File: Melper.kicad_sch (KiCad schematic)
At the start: 41 parts, among them J1 Conn_01x02, J2 Conn_02x08_Odd_Even, J3 Conn_02x08_Odd_Even, J4 Conn_02x08_Odd_Even, J5 Conn_02x08_Odd_Even, J6 Conn_02x08_Odd_Even, U1 LM7805_TO220, U2 cui

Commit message: Update Melper.kicad_sch
Changes LED resistors.
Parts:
- J1: Digi-Key Part 2987-CI3102P1V00-NH-ND -> 900-0022232021-ND
- R1, R3: value 1K -> 10K; Digi-Key Part CF14JT1K00CT-ND -> S10KQCT-ND
- R2: value 1K -> 4.7K; Digi-Key Part CF14JT1K00CT-ND -> S4.7KQCT-ND
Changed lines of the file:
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@@
       (effects (font (size 1.27 1.27)) hide)
     )
-    (property "Digi-Key Part" "2987-CI3102P1V00-NH-ND" (id 4) (at 37.465 47.625 0)
+    (property "Digi-Key Part" "900-0022232021-ND" (id 4) (at 37.465 47.625 0)
+      (effects (font (size 1.27 1.27)) hide)
+    )
+    (property "LCSC Part #" "" (id 5) (at 37.465 47.625 0)
       (effects (font (size 1.27 1.27)) hide)
     )
@@
       (effects (font (size 1.27 1.27)) (justify left))
     )
-    (property "Value" "1K" (id 1) (at 138.811 113.6266 0)
+    (property "Value" "4.7K" (id 1) (at 138.811 113.6266 0)
       (effects (font (size 1.27 1.27)) (justify left))
     )
@@
       (effects (font (size 1.27 1.27)) hide)
     )
-    (property "Digi-Key Part" "CF14JT1K00CT-ND" (id 4) (at 137.16 111.76 0)
+    (property "Digi-Key Part" "S4.7KQCT-ND" (id 4) (at 137.16 111.76 0)
       (effects (font (size 1.27 1.27)) hide)
     )
@@
       (effects (font (size 1.27 1.27)) (justify left))
     )
-    (property "Value" "1K" (id 1) (at 122.936 113.6266 0)
+    (property "Value" "10K" (id 1) (at 122.936 113.6266 0)
       (effects (font (size 1.27 1.27)) (justify left))
     )
@@
       (effects (font (size 1.27 1.27)) hide)
     )
-    (property "Digi-Key Part" "CF14JT1K00CT-ND" (id 4) (at 121.285 111.76 0)
+    (property "Digi-Key Part" "S10KQCT-ND" (id 4) (at 121.285 111.76 0)
       (effects (font (size 1.27 1.27)) hide)
     )
@@
       (effects (font (size 1.27 1.27)) (justify left))
     )
-    (property "Value" "1K" (id 1) (at 157.226 113.6266 0)
+    (property "Value" "10K" (id 1) (at 157.226 113.6266 0)
       (effects (font (size 1.27 1.27)) (justify left))
     )
@@
       (effects (font (size 1.27 1.27)) hide)
     )
-    (property "Digi-Key Part" "CF14JT1K00CT-ND" (id 4) (at 155.575 111.76 0)
+    (property "Digi-Key Part" "S10KQCT-ND" (id 4) (at 155.575 111.76 0)
       (effects (font (size 1.27 1.27)) hide)
     )
@@
     )
     (path "/a8dccc38-b961-440c-b049-c49b742a9e52"
-      (reference "R1") (unit 1) (value "1K") (footprint "Resistor_THT:R_Axial_DIN0207_L6.3mm_D2.5mm_P10.16mm_Horizontal")
+      (reference "R1") (unit 1) (value "10K") (footprint "Resistor_THT:R_Axial_DIN0207_L6.3mm_D2.5mm_P10.16mm_Horizontal")
     )
     (path "/6bd6e3e5-09a1-47fe-8dda-35283554daae"
-      (reference "R2") (unit 1) (value "1K") (footprint "Resistor_THT:R_Axial_DIN0207_L6.3mm_D2.5mm_P10.16mm_Horizontal")
+      (reference "R2") (unit 1) (value "4.7K") (footprint "Resistor_THT:R_Axial_DIN0207_L6.3mm_D2.5mm_P10.16mm_Horizontal")
     )
     (path "/efc05906-5544-4847-b5a7-fc1758017ed4"
-      (reference "R3") (unit 1) (value "1K") (footprint "Resistor_THT:R_Axial_DIN0207_L6.3mm_D2.5mm_P10.16mm_Horizontal")
+      (reference "R3") (unit 1) (value "10K") (footprint "Resistor_THT:R_Axial_DIN0207_L6.3mm_D2.5mm_P10.16mm_Horizontal")
     )
     (path "/46d42ec2-41a1-4900-9741-6b632d1e4aaf"

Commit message: Version 2.1
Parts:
- removed C10, C11, C12, C13, C14, C15, C16, C17, C18, C19, C20, C21, C5, C7, C8, C9: .1uF, Capacitor_THT:C_Disc_D4.3mm_W1.9mm_P5.00mm, symbol Device:C_Small
- added C5, C7: 10uF, Capacitor_THT:CP_Radial_D8.0mm_P5.00mm, symbol Device:C_Polarized_Small_US
- C1: value .33uF -> 10uF; footprint Capacitor_THT:C_Disc_D4.3mm_W1.9mm_P5.00mm -> Capacitor_THT:CP_Radial_D8.0mm_P5.00mm; symbol Device:C_Small -> Device:C_Polarized_Small_US; Digi-Key Part 445-173446-1-ND -> 399-20957-1-ND
- C2: footprint Capacitor_THT:CP_Radial_Tantal_D5.0mm_P5.00mm -> Capacitor_THT:CP_Radial_D8.0mm_P5.00mm; Digi-Key Part 478-TAP106K016CRSCT-ND -> 399-20957-1-ND
- C6: value 22uF -> 10uF; footprint Capacitor_THT:CP_Radial_Tantal_D6.0mm_P5.00mm -> Capacitor_THT:CP_Radial_D8.0mm_P5.00mm; Digi-Key Part 478-7373-1-ND -> 399-20957-1-ND
- R2: Digi-Key Part S4.7KQCT-ND -> CF14JT4K70CT-ND
- U1: footprint Package_TO_SOT_THT:TO-220-3_Vertical -> Package_TO_SOT_THT:TO-220-3_Horizontal_TabDown
- U2: value cui -> VXO78012-1000
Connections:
- net +12V: now also C7.1
- net -12V: now also C5.2
- net GND: now also C5.1, C7.2
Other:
- moved on the sheet: J1

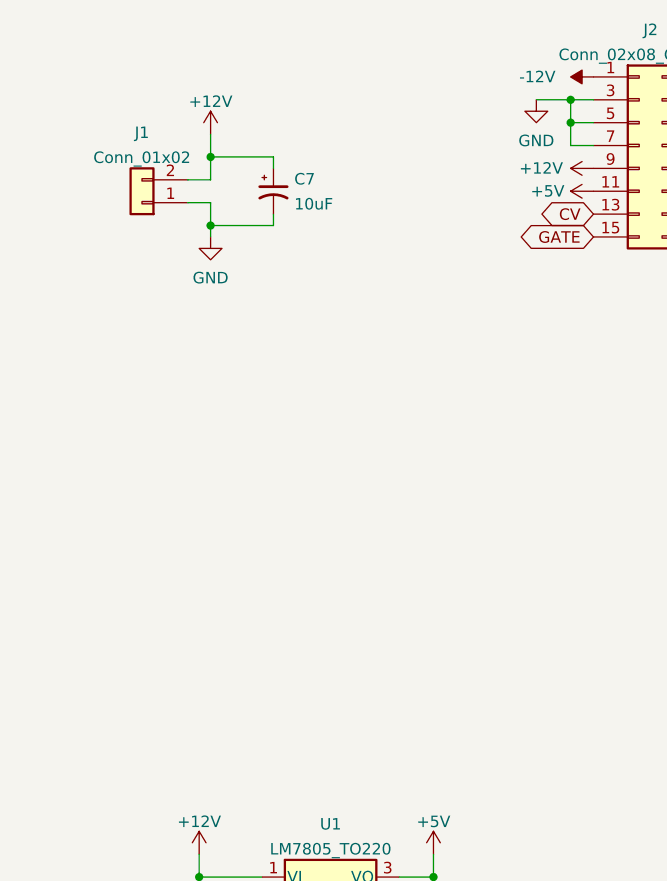
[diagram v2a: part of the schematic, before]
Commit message: Version 3
Adds 6th power connector.
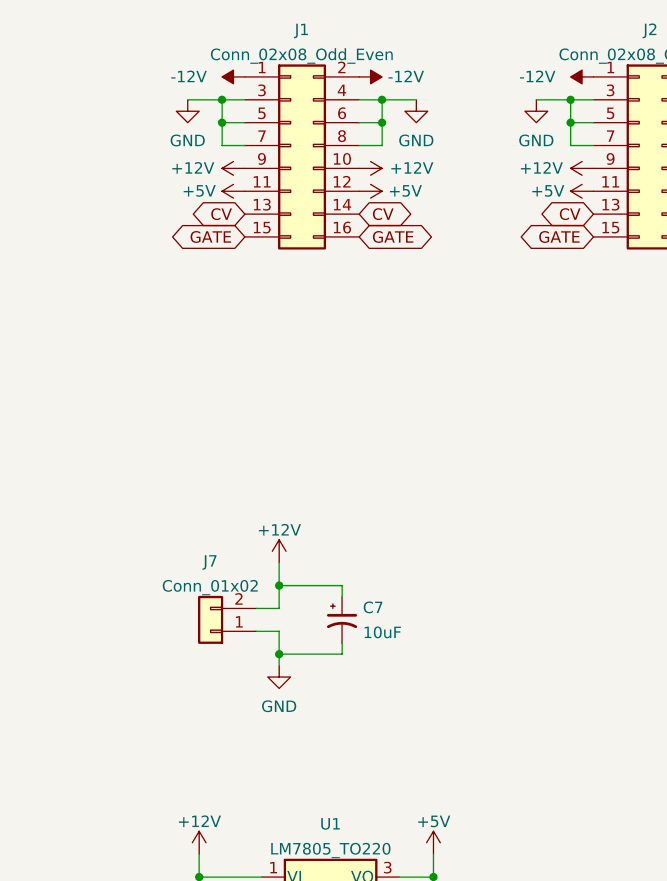
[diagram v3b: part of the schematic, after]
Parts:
- added J1: Conn_02x08_Odd_Even, Connector_PinHeader_2.54mm:PinHeader_2x08_P2.54mm_Vertical, symbol Connector_Generic:Conn_02x08_Odd_Even
- renumbered J1 to J7
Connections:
- net +12V: now also J1.10 (Pin_10), J1.9 (Pin_9)
- net +5V: now also J1.11 (Pin_11), J1.12 (Pin_12)
- net -12V: now also J1.1 (Pin_1), J1.2 (Pin_2)
- net CV: now also J1.13 (Pin_13), J1.14 (Pin_14)
- net GATE: now also J1.15 (Pin_15), J1.16 (Pin_16)
- net GND: now also J1.3 (Pin_3), J1.4 (Pin_4), J1.5 (Pin_5), J1.6 (Pin_6), J1.7 (Pin_7), J1.8 (Pin_8)
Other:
- moved on the sheet: C7, J7

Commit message: Rev 3.2
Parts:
- added TP2, TP3, TP4: TestPoint, TestPoint:TestPoint_Pad_D2.0mm, symbol Connector:TestPoint
- TP1: Digi-Key Part (none) -> 36-5006-ND
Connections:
- net +12V: now also TP2.1
- net +5V: now also TP3.1
- net -12V: now also TP4.1
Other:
- moved on the sheet: TP1

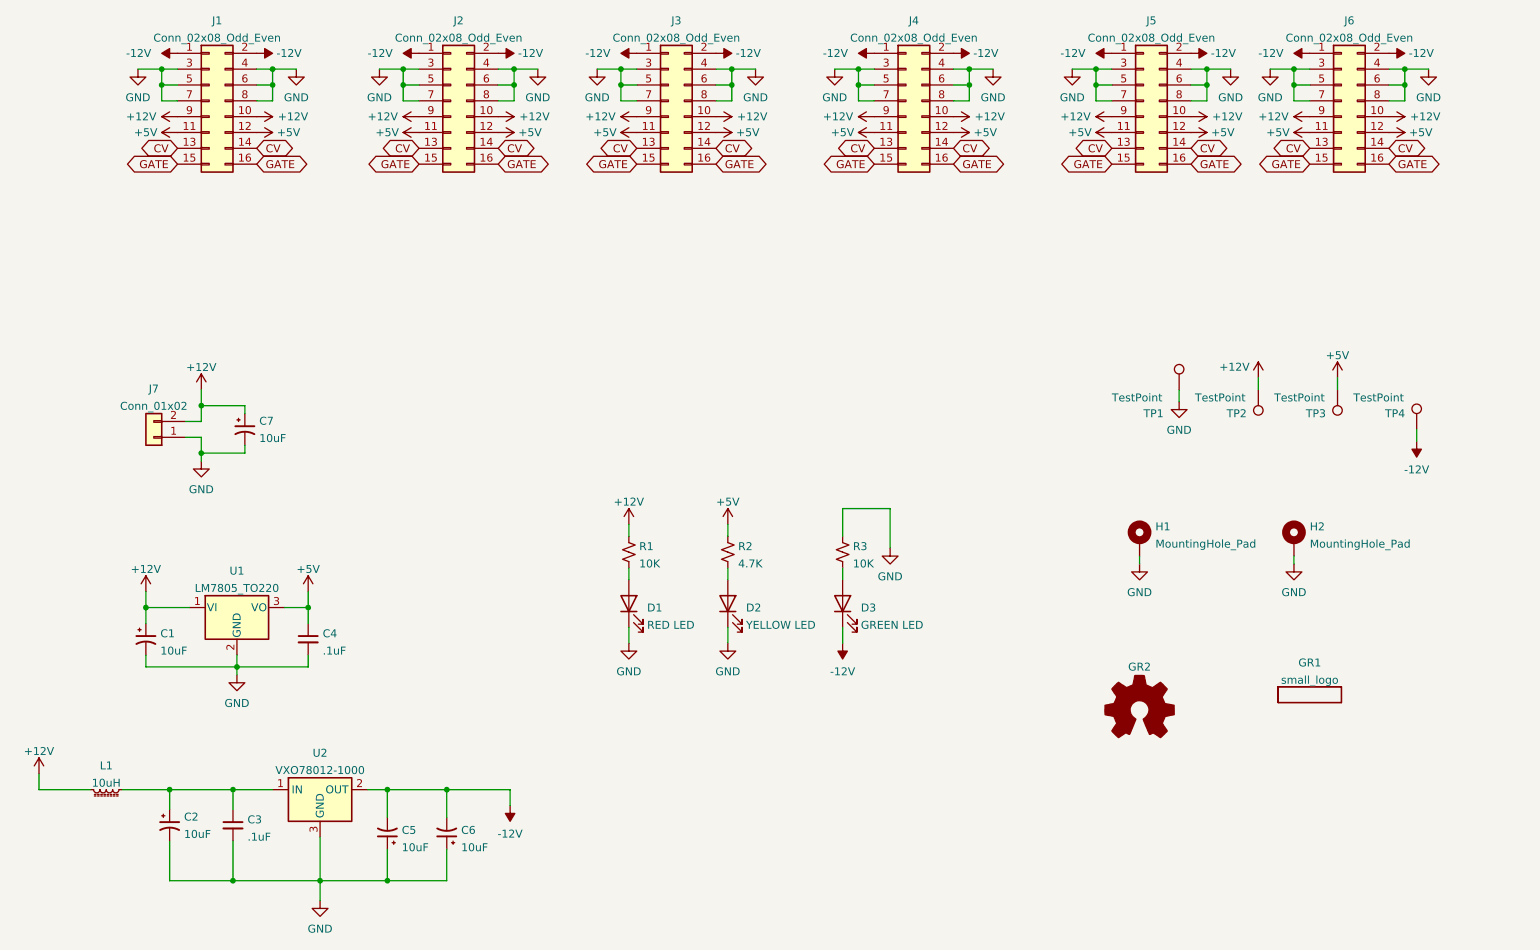
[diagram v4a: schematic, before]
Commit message: Revision 3.5
Changes negative regulator.
Adds support for JLC build.
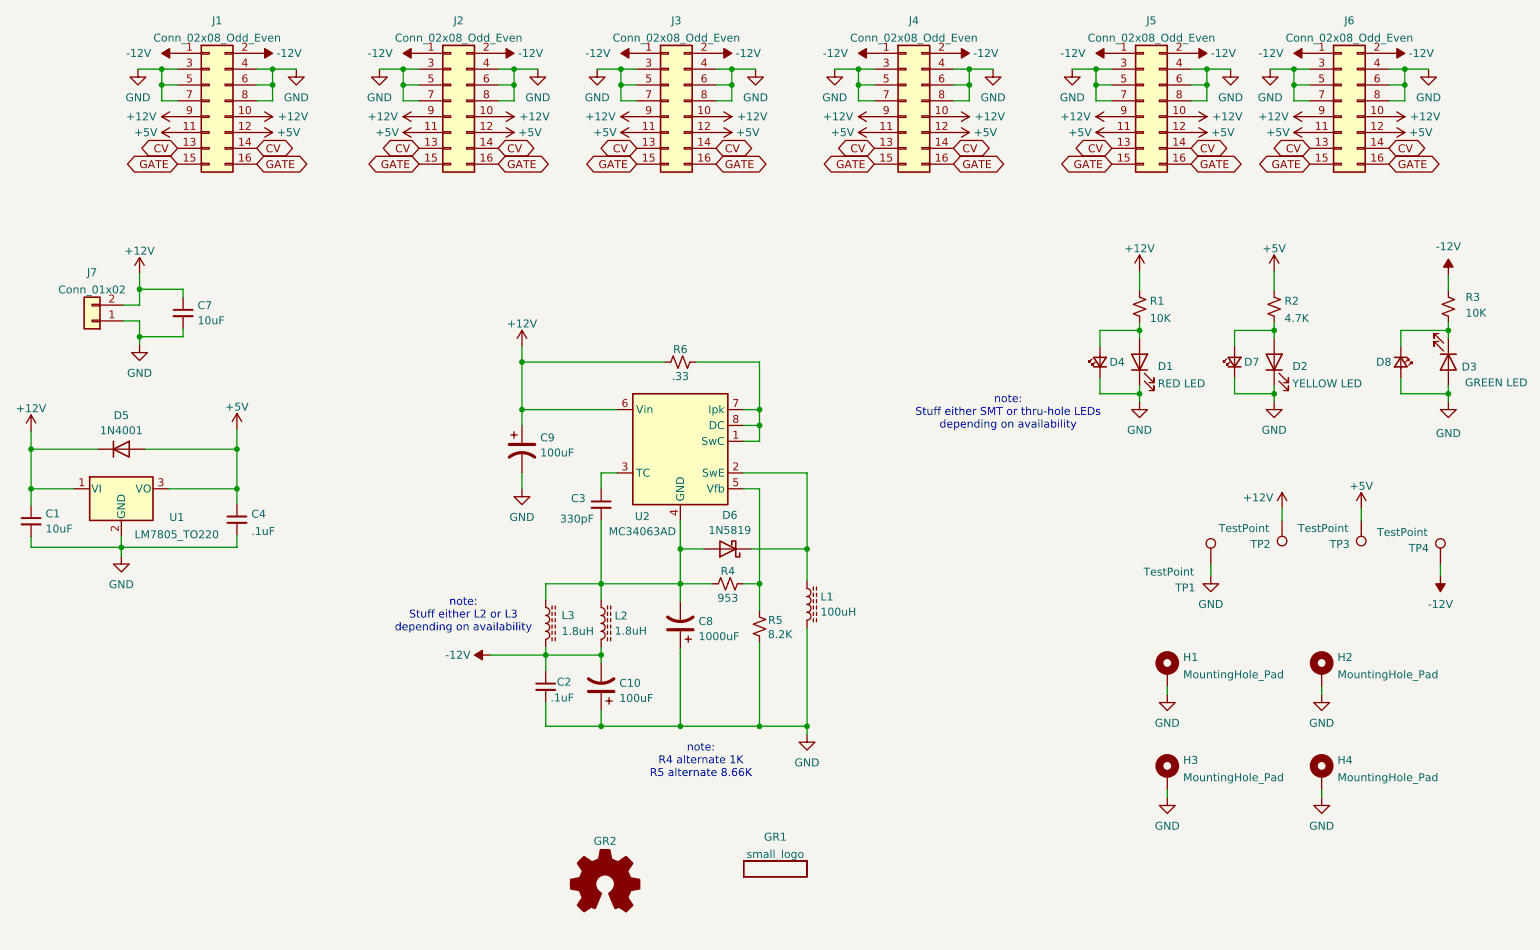
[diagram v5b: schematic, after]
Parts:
- removed C2, C5, C6: 10uF, Capacitor_THT:CP_Radial_D8.0mm_P5.00mm, symbol Device:C_Polarized_Small_US
- removed L1: 10uH, Inductor_THT:L_Radial_D8.7mm_P5.00mm_Fastron_07HCP, symbol Device:L_Ferrite_Small
- removed U2: VXO78012-1000, Converter_DCDC:Converter_DCDC_Murata_OKI-78SR_Vertical, symbol greenface-symbols:cui
- added C10, C9: 100uF, Capacitor_THT:CP_Radial_D6.3mm_P2.50mm, symbol Device:C_Polarized_US
- added C2: .1uF, Capacitor_THT:C_Disc_D4.3mm_W1.9mm_P5.00mm, symbol Device:C_Small
- added C8: 1000uF, Capacitor_THT:CP_Radial_D10.0mm_P5.00mm, symbol Device:C_Polarized_US
- added D4: Red SMT LED, LED_SMD:LED_0603_1608Metric_Pad1.05x0.95mm_HandSolder, symbol Device:LED_Small
- added D5: 1N4001, Diode_THT:D_DO-41_SOD81_P10.16mm_Horizontal, symbol Diode:1N4001
- added D6: 1N5819, Diode_THT:D_DO-41_SOD81_P7.62mm_Horizontal, symbol Device:D_Schottky
- added D7: Yellow SMT LED, LED_SMD:LED_0603_1608Metric_Pad1.05x0.95mm_HandSolder, symbol Device:LED_Small
- added D8: Blue SMT LED, LED_SMD:LED_0603_1608Metric_Pad1.05x0.95mm_HandSolder, symbol Device:LED_Small
- added H3, H4: MountingHole_Pad, MountingHole:MountingHole_3.2mm_M3_DIN965_Pad, symbol Mechanical:MountingHole_Pad
- added L1: 100uH, Inductor_THT:L_Radial_D8.7mm_P5.00mm_Fastron_07HCP, symbol Device:L_Ferrite
- added L2: 1.8uH, Inductor_THT:L_Axial_L9.5mm_D4.0mm_P12.70mm_Horizontal_Fastron_SMCC, symbol Device:L_Ferrite
- added L3: 1.8uH, Inductor_SMD:L_Sunlord_SWPA4012S, symbol Device:L_Ferrite
- added R4: 953, Resistor_THT:R_Axial_DIN0207_L6.3mm_D2.5mm_P10.16mm_Horizontal, symbol Device:R_Small_US
- added R5: 8.2K, Resistor_THT:R_Axial_DIN0207_L6.3mm_D2.5mm_P10.16mm_Horizontal, symbol Device:R_Small_US
- added R6: .33, Resistor_THT:R_Axial_DIN0207_L6.3mm_D2.5mm_P10.16mm_Horizontal, symbol Device:R_Small_US
- added U2: MC34063AD, Package_DIP:DIP-8_W7.62mm_LongPads, symbol Regulator_Switching:MC34063AD
- C1, C7: footprint Capacitor_THT:CP_Radial_D8.0mm_P5.00mm -> Capacitor_THT:C_Disc_D5.1mm_W3.2mm_P5.00mm; symbol Device:C_Polarized_Small_US -> Device:C_Small; Digi-Key Part 399-20957-1-ND -> 445-173437-1-ND; LCSC Part # (none) -> C531341
- C3: value .1uF -> 330pF; Digi-Key Part 399-9877-1-ND -> 399-4231-ND; LCSC Part # (none) -> C2896045
- C4: LCSC Part # (none) -> C84772
- J1, J2, J3, J4, J5, J6: LCSC Part # (none) -> C305956
- J7: LCSC Part # (none) -> C2905434
- R1, R3: LCSC Part # (none) -> C57436
- R2: LCSC Part # (none) -> C176521
- TP1: LCSC Part # (none) -> C238124
- TP2, TP3, TP4: Digi-Key Part 36-5006-ND -> (none)
- U1: LCSC Part # (none) -> C111887
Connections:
- net +12V: now also C9.1, D5.1 (K), R6.1, U2.6 (Vin)
- net +5V: now also D5.2 (A)
- net -12V: now also R3.2, C10.2, C2.1, L2.2, L3.2; no longer D3.1 (K)
- net GND: now also D3.2 (A), C10.1, C2.2, C8.1, C9.2, D4.1 (K), D7.1 (K), D8.2 (A), H3.1, H4.1, L1.2, R5.1; no longer C3.2, R3.1
- net at D2.2 (A), R2.2: now also D7.2 (A)
- net at C3.1: now also U2.3 (TC)
- net at D1.2 (A), R1.2: now also D4.2 (A)
- new net: D3.1 (K), D8.1 (K), R3.1
- new net: C3.2, C8.2, D6.2 (A), L2.1, L3.1, R4.1, U2.4 (GND)
- new net: D6.1 (K), L1.1, U2.2 (SwE)
- new net: R6.2, U2.1 (SwC), U2.7 (Ipk), U2.8 (DC)
- new net: R4.2, R5.2, U2.5 (Vfb)
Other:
- note added: "note: R4 alternate 1K R5 alternate 8.66K"
- note added: "note: Stuff either L2 or L3 depending on availability"
- note added: "note: Stuff either SMT or thru-hole LEDs depending on availability"
- moved on the sheet: C4, D1, D2, D3, GR1, GR2, H1, H2, J7, R1, R2, R3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
